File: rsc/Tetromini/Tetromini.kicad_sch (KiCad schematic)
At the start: 8 parts

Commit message: improved schematics, added readme
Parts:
- DOWN1, LEFT1, RIGHT1, ROT_LEFT1, ROT_RIGHT1, UP1: DigiKey_PN (none) -> 679-2442-ND; MPN (none) -> MJTP1234; Manufacturer (none) -> APEM Inc.
- DS1: DigiKey_PN (none) -> --; MPN (none) -> --; Manufacturer (none) -> HiLetgo
- U1: renamed from U2; DigiKey_PN (none) -> 1528-2828-ND; MPN (none) -> 4062; Manufacturer (none) -> Adafruit

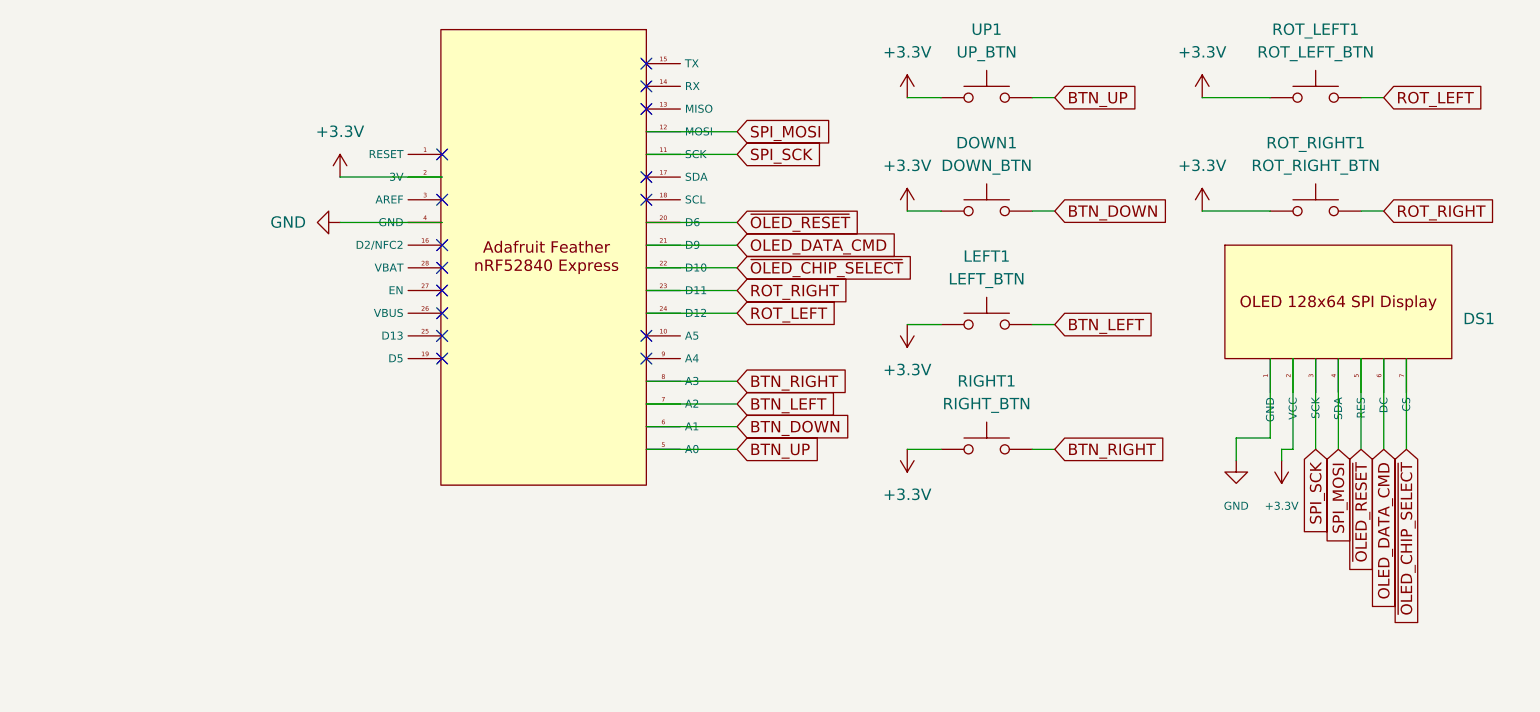
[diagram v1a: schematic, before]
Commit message: Added main menu, inputs handled via ring buffer, battery status queried in threat with mutexed vars, shutdown added!
BEEFY COMMIT!!! YAY!!! I now kinda understand a bit more about atomics and mutexes and ring buffers and a smidge of semaphores too!! Huzzah!
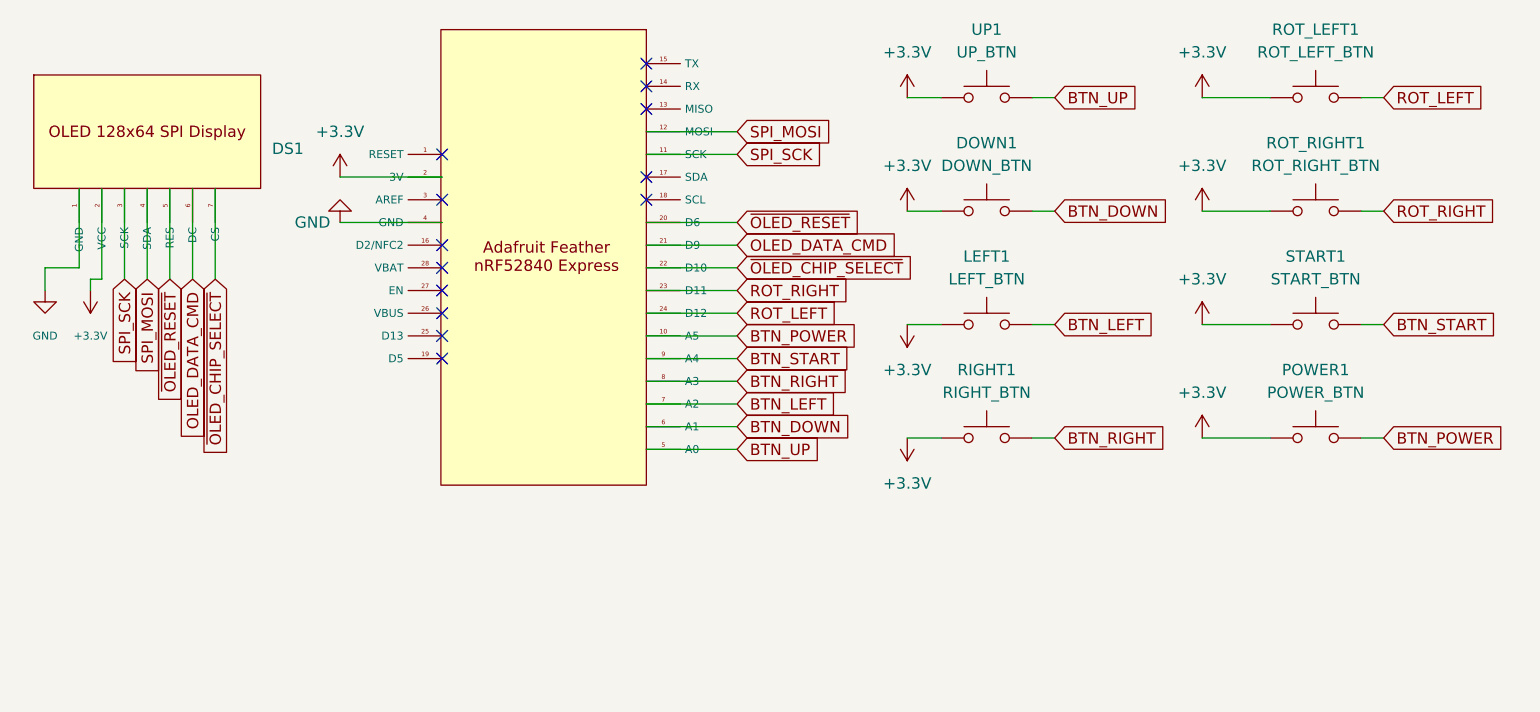
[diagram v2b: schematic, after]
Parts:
- added POWER1: POWER_BTN, symbol Switch:SW_Push
- added START1: START_BTN, symbol Switch:SW_Push
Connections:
- net +3.3V: now also POWER1.1, START1.1
- net BTN_POWER: now reaches U1.10 (A5)
- net BTN_POWER: now also POWER1.2
- net BTN_START: now reaches U1.9 (A4)
- net BTN_START: now also START1.2
- no-connect marks 15 -> 13
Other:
- moved on the sheet: DS1, RIGHT1
